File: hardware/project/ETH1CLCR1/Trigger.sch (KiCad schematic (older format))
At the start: 17 parts, among them U401 74AC125, U402 ADuM5402

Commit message: Footprint asigment (not finished).
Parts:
- C402, C404: footprint Capacitor_SMD:C_0603_1608Metric_Pad1.05x0.95mm_HandSolder -> Capacitor_SMD:C_0805_2012Metric_Pad1.15x1.40mm_HandSolder
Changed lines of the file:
@@
 F 0 "C402" H 4465 1196 50  0000 L CNN
 F 1 "1u" H 4465 1105 50  0000 L CNN
-F 2 "Capacitor_SMD:C_0603_1608Metric_Pad1.05x0.95mm_HandSolder" H 4388 1000 50  0001 C CNN
+F 2 "Capacitor_SMD:C_0805_2012Metric_Pad1.15x1.40mm_HandSolder" H 4388 1000 50  0001 C CNN
 F 3 "~" H 4350 1150 50  0001 C CNN
 	1    4350 1150
@@
 F 0 "C404" H 6165 1196 50  0000 L CNN
 F 1 "1u" H 6165 1105 50  0000 L CNN
-F 2 "Capacitor_SMD:C_0603_1608Metric_Pad1.05x0.95mm_HandSolder" H 6088 1000 50  0001 C CNN
+F 2 "Capacitor_SMD:C_0805_2012Metric_Pad1.15x1.40mm_HandSolder" H 6088 1000 50  0001 C CNN
 F 3 "~" H 6050 1150 50  0001 C CNN
 	1    6050 1150

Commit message: Modification in schematic and PCB layout.
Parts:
- added C407, C408: 100n, Capacitor_SMD:C_0603_1608Metric_Pad1.05x0.95mm_HandSolder, symbol Device:C
- added R406: 10k, Resistor_SMD:R_0603_1608Metric_Pad1.05x0.95mm_HandSolder, symbol Device:R
- added U403: TXB0104PW, Package_SO:TSSOP-14_4.4x5mm_P0.65mm, symbol Logic_LevelTranslator:TXB0104PW
- C402, C404: footprint Capacitor_SMD:C_0805_2012Metric_Pad1.15x1.40mm_HandSolder -> Capacitor_SMD:C_0603_1608Metric_Pad1.05x0.95mm_HandSolder
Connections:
- net +3V3: now also C408.1, R406.1, U403.1 (VCCA); no longer C401.1, C402.1, U402.1 (VDD1)
- net GND: now also C407.2, C408.2, U403.7 (GND)
- net TRIG_EN: now also U403.2 (A1); no longer U402.3 (VIA)
- net TRIG_IN: now also U403.4 (A3); no longer U402.5 (VOC)
- net TRIG_OUT: now also U403.3 (A2); no longer U402.4 (VIB)
- new net: U402.3 (VIA), U403.13 (B1)
- new net: U402.4 (VIB), U403.12 (B2)
- new net: U402.5 (VOC), U403.11 (B3)
- new net: R406.2, U403.8 (OE)
- new net +5V: C401.1, C402.1, C407.1, U402.1 (VDD1), U403.14 (VCCB)
- no-connect marks 3 -> 5
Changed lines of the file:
@@
 Wire Wire Line
 	5800 3250 5200 3250
-Text HLabel 4100 3050 0    50   Input ~ 0
+Text HLabel 2650 3050 0    50   Input ~ 0
 TRIG_EN
-Text HLabel 4100 3150 0    50   Input ~ 0
+Text HLabel 2650 3250 0    50   Input ~ 0
 TRIG_OUT
-Text HLabel 4100 3250 0    50   Output ~ 0
+Text HLabel 2650 3450 0    50   Output ~ 0
 TRIG_IN
 Wire Notes Line
@@
 F 0 "C402" H 4465 1196 50  0000 L CNN
 F 1 "1u" H 4465 1105 50  0000 L CNN
-F 2 "Capacitor_SMD:C_0805_2012Metric_Pad1.15x1.40mm_HandSolder" H 4388 1000 50  0001 C CNN
+F 2 "Capacitor_SMD:C_0603_1608Metric_Pad1.05x0.95mm_HandSolder" H 4388 1000 50  0001 C CNN
 F 3 "~" H 4350 1150 50  0001 C CNN
 	1    4350 1150
-	-1   0    0    -1
+	1    0    0    -1
 $EndComp
 $Comp
@@
 F 3 "~" H 3850 1150 50  0001 C CNN
 	1    3850 1150
-	-1   0    0    -1
+	1    0    0    -1
 $EndComp
 Wire Wire Line
@@
 F 0 "C404" H 6165 1196 50  0000 L CNN
 F 1 "1u" H 6165 1105 50  0000 L CNN
-F 2 "Capacitor_SMD:C_0805_2012Metric_Pad1.15x1.40mm_HandSolder" H 6088 1000 50  0001 C CNN
+F 2 "Capacitor_SMD:C_0603_1608Metric_Pad1.05x0.95mm_HandSolder" H 6088 1000 50  0001 C CNN
 F 3 "~" H 6050 1150 50  0001 C CNN
 	1    6050 1150
@@
 	5800 1350 5550 1350
 Wire Wire Line
-	4100 3050 4200 3050
-Wire Wire Line
-	4100 3150 4200 3150
-Wire Wire Line
-	4100 3250 4200 3250
+	2650 3050 2750 3050
+Wire Wire Line
+	2650 3250 2750 3250
+Wire Wire Line
+	2650 3450 2750 3450
 $Comp
 L Device:C C405
@@
 NoConn ~ 4200 3550
 $Comp
-L power:+3.3V #PWR0407
-U 1 1 5EBBBCC5
-P 4500 2650
-F 0 "#PWR0407" H 4500 2500 50  0001 C CNN
-F 1 "+3.3V" H 4515 2823 50  0000 C CNN
-F 2 "" H 4500 2650 50  0001 C CNN
-F 3 "" H 4500 2650 50  0001 C CNN
-	1    4500 2650
-	1    0    0    -1
-$EndComp
-$Comp
-L power:+3.3V #PWR0401
-U 1 1 5EBBC990
-P 4100 900
-F 0 "#PWR0401" H 4100 750 50  0001 C CNN
-F 1 "+3.3V" H 4115 1073 50  0000 C CNN
-F 2 "" H 4100 900 50  0001 C CNN
-F 3 "" H 4100 900 50  0001 C CNN
-	1    4100 900
-	1    0    0    -1
-$EndComp
-$Comp
 L power:GND #PWR0404
 U 1 1 5EBCD574
@@
 	1    0    0    -1
 $EndComp
+$Comp
+L Logic_LevelTranslator:TXB0104PW U?
+U 1 1 5E35DAF4
+P 3150 3350
+AR Path="/5DEEF70B/5E35DAF4" Ref="U?"  Part="1"
+AR Path="/5DEA9498/5E35DAF4" Ref="U403"  Part="1"
+F 0 "U403" H 3650 4100 50  0000 C CNN
+F 1 "TXB0104PW" H 3650 4000 50  0000 C CNN
+F 2 "Package_SO:TSSOP-14_4.4x5mm_P0.65mm" H 3150 2600 50  0001 C CNN
+F 3 "http://www.ti.com/lit/ds/symlink/txb0104.pdf" H 3260 3445 50  0001 C CNN
+	1    3150 3350
+	1    0    0    -1
+$EndComp
+NoConn ~ 2750 3650
+NoConn ~ 3550 3650
+$Comp
+L Device:R R?
+U 1 1 5E35DB02
+P 2550 2650
+AR Path="/5DEEF70B/5E35DB02" Ref="R?"  Part="1"
+AR Path="/5DEA9498/5E35DB02" Ref="R406"  Part="1"
+F 0 "R406" H 2480 2696 50  0000 R CNN
+F 1 "10k" H 2480 2605 50  0000 R CNN
+F 2 "Resistor_SMD:R_0603_1608Metric_Pad1.05x0.95mm_HandSolder" V 2480 2650 50  0001 C CNN
+F 3 "~" H 2550 2650 50  0001 C CNN
+	1    2550 2650
+	1    0    0    -1
+$EndComp
+Wire Wire Line
+	3050 2650 3050 2600
+Wire Wire Line
+	3050 2600 2950 2600
+Wire Wire Line
+	2950 2600 2950 2550
+Wire Wire Line
+	3250 2650 3250 2600
+Wire Wire Line
+	3250 2600 3350 2600
+Wire Wire Line
+	3350 2600 3350 2550
+Wire Wire Line
+	2750 2850 2550 2850
+Wire Wire Line
+	2550 2850 2550 2800
+$Comp
+L power:+3.3V #PWR0407
+U 1 1 5E3798C8
+P 2950 2550
+F 0 "#PWR0407" H 2950 2400 50  0001 C CNN
+F 1 "+3.3V" H 2965 2723 50  0000 C CNN
+F 2 "" H 2950 2550 50  0001 C CNN
+F 3 "" H 2950 2550 50  0001 C CNN
+	1    2950 2550
+	1    0    0    -1
+$EndComp
+$Comp
+L power:+3.3V #PWR0401
+U 1 1 5E37A16A
+P 2550 2500
+F 0 "#PWR0401" H 2550 2350 50  0001 C CNN
+F 1 "+3.3V" H 2565 2673 50  0000 C CNN
+F 2 "" H 2550 2500 50  0001 C CNN
+F 3 "" H 2550 2500 50  0001 C CNN
+	1    2550 2500
+	1    0    0    -1
+$EndComp
+$Comp
+L Device:C C407
+U 1 1 5E381279
+P 2850 1150
+F 0 "C407" H 2965 1196 50  0000 L CNN
+F 1 "100n" H 2965 1105 50  0000 L CNN
+F 2 "Capacitor_SMD:C_0603_1608Metric_Pad1.05x0.95mm_HandSolder" H 2888 1000 50  0001 C CNN
+F 3 "~" H 2850 1150 50  0001 C CNN
+	1    2850 1150
+	1    0    0    -1
+$EndComp
+$Comp
+L Device:C C408
+U 1 1 5E381C99
+P 3350 1150
+F 0 "C408" H 3465 1196 50  0000 L CNN
+F 1 "100n" H 3465 1105 50  0000 L CNN
+F 2 "Capacitor_SMD:C_0603_1608Metric_Pad1.05x0.95mm_HandSolder" H 3388 1000 50  0001 C CNN
+F 3 "~" H 3350 1150 50  0001 C CNN
+	1    3350 1150
+	1    0    0    -1
+$EndComp
+$Comp
+L power:+3.3V #PWR0426
+U 1 1 5E387028
+P 3350 900
+F 0 "#PWR0426" H 3350 750 50  0001 C CNN
+F 1 "+3.3V" H 3365 1073 50  0000 C CNN
+F 2 "" H 3350 900 50  0001 C CNN
+F 3 "" H 3350 900 50  0001 C CNN
+	1    3350 900
+	1    0    0    -1
+$EndComp
+$Comp
+L power:GND #PWR0427
+U 1 1 5E38746C
+P 3350 1400
+F 0 "#PWR0427" H 3350 1150 50  0001 C CNN
+F 1 "GND" H 3355 1227 50  0000 C CNN
+F 2 "" H 3350 1400 50  0001 C CNN
+F 3 "" H 3350 1400 50  0001 C CNN
+	1    3350 1400
+	1    0    0    -1
+$EndComp
+Wire Wire Line
+	3350 900  3350 1000
+Wire Wire Line
+	3350 1300 3350 1400
+$Comp
+L power:+5V #PWR0429
+U 1 1 5E38BA23
+P 4500 2650
+F 0 "#PWR0429" H 4500 2500 50  0001 C CNN
+F 1 "+5V" H 4515 2823 50  0000 C CNN
+F 2 "" H 4500 2650 50  0001 C CNN
+F 3 "" H 4500 2650 50  0001 C CNN
+	1    4500 2650
+	1    0    0    -1
+$EndComp
+$Comp
+L power:+5V #PWR0425
+U 1 1 5E38BD2A
+P 3350 2550
+F 0 "#PWR0425" H 3350 2400 50  0001 C CNN
+F 1 "+5V" H 3365 2723 50  0000 C CNN
+F 2 "" H 3350 2550 50  0001 C CNN
+F 3 "" H 3350 2550 50  0001 C CNN
+	1    3350 2550
+	1    0    0    -1
+$EndComp
+$Comp
+L power:+5V #PWR0423
+U 1 1 5E38C131
+P 2850 900
+F 0 "#PWR0423" H 2850 750 50  0001 C CNN
+F 1 "+5V" H 2865 1073 50  0000 C CNN
+F 2 "" H 2850 900 50  0001 C CNN
+F 3 "" H 2850 900 50  0001 C CNN
+	1    2850 900
+	1    0    0    -1
+$EndComp
+$Comp
+L power:+5V #PWR0428
+U 1 1 5E38CD59
+P 4100 900
+F 0 "#PWR0428" H 4100 750 50  0001 C CNN
+F 1 "+5V" H 4115 1073 50  0000 C CNN
+F 2 "" H 4100 900 50  0001 C CNN
+F 3 "" H 4100 900 50  0001 C CNN
+	1    4100 900
+	1    0    0    -1
+$EndComp
+$Comp
+L power:GND #PWR0424
+U 1 1 5E38D207
+P 2850 1400
+F 0 "#PWR0424" H 2850 1150 50  0001 C CNN
+F 1 "GND" H 2855 1227 50  0000 C CNN
+F 2 "" H 2850 1400 50  0001 C CNN
+F 3 "" H 2850 1400 50  0001 C CNN
+	1    2850 1400
+	1    0    0    -1
+$EndComp
+Wire Wire Line
+	2850 1400 2850 1300
+Wire Wire Line
+	2850 1000 2850 900
+$Comp
+L power:GND #PWR0106
+U 1 1 5E39EC61
+P 3150 4050
+F 0 "#PWR0106" H 3150 3800 50  0001 C CNN
+F 1 "GND" H 3155 3877 50  0000 C CNN
+F 2 "" H 3150 4050 50  0001 C CNN
+F 3 "" H 3150 4050 50  0001 C CNN
+	1    3150 4050
+	1    0    0    -1
+$EndComp
+Wire Wire Line
+	3550 3050 4200 3050
+Wire Wire Line
+	4200 3150 3700 3150
+Wire Wire Line
+	3700 3150 3700 3250
+Wire Wire Line
+	3700 3250 3550 3250
+Wire Wire Line
+	3550 3450 3800 3450
+Wire Wire Line
+	3800 3450 3800 3250
+Wire Wire Line
+	3800 3250 4200 3250
 $EndSCHEMATC

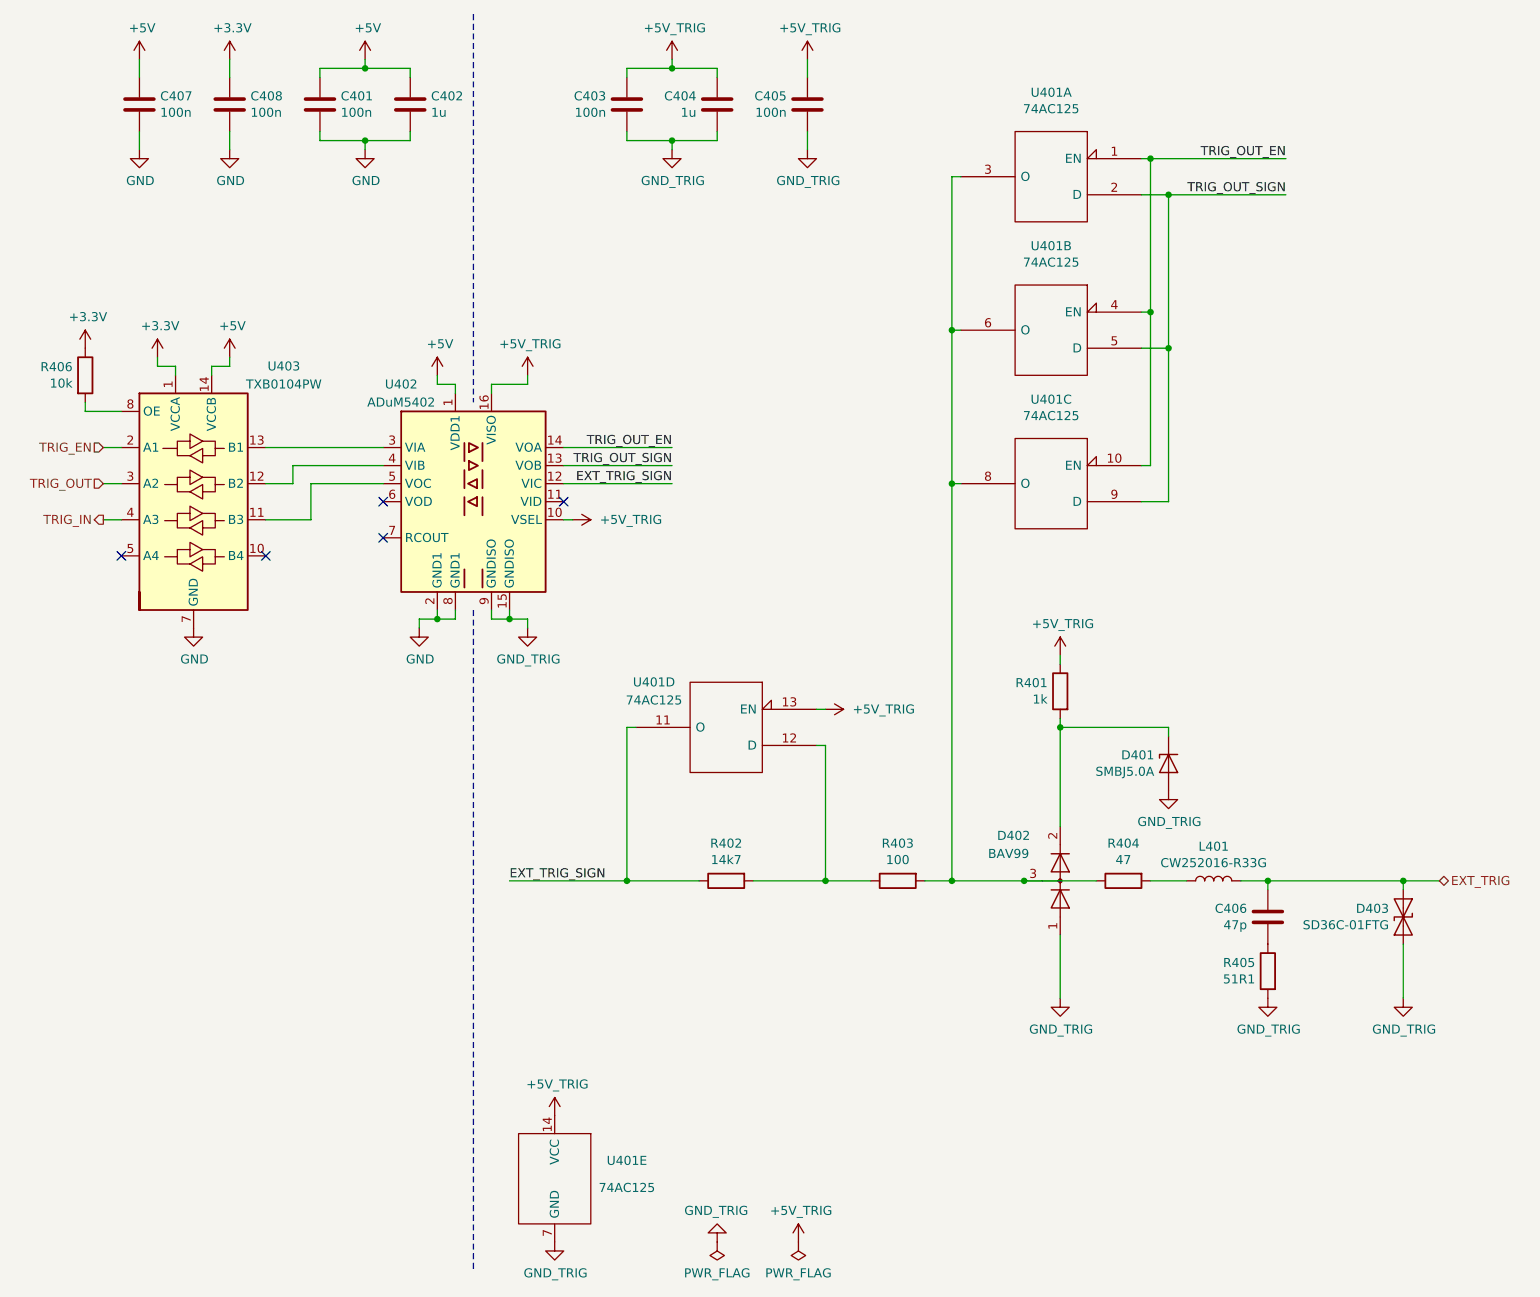
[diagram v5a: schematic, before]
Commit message: Redesinged ADC schematic.
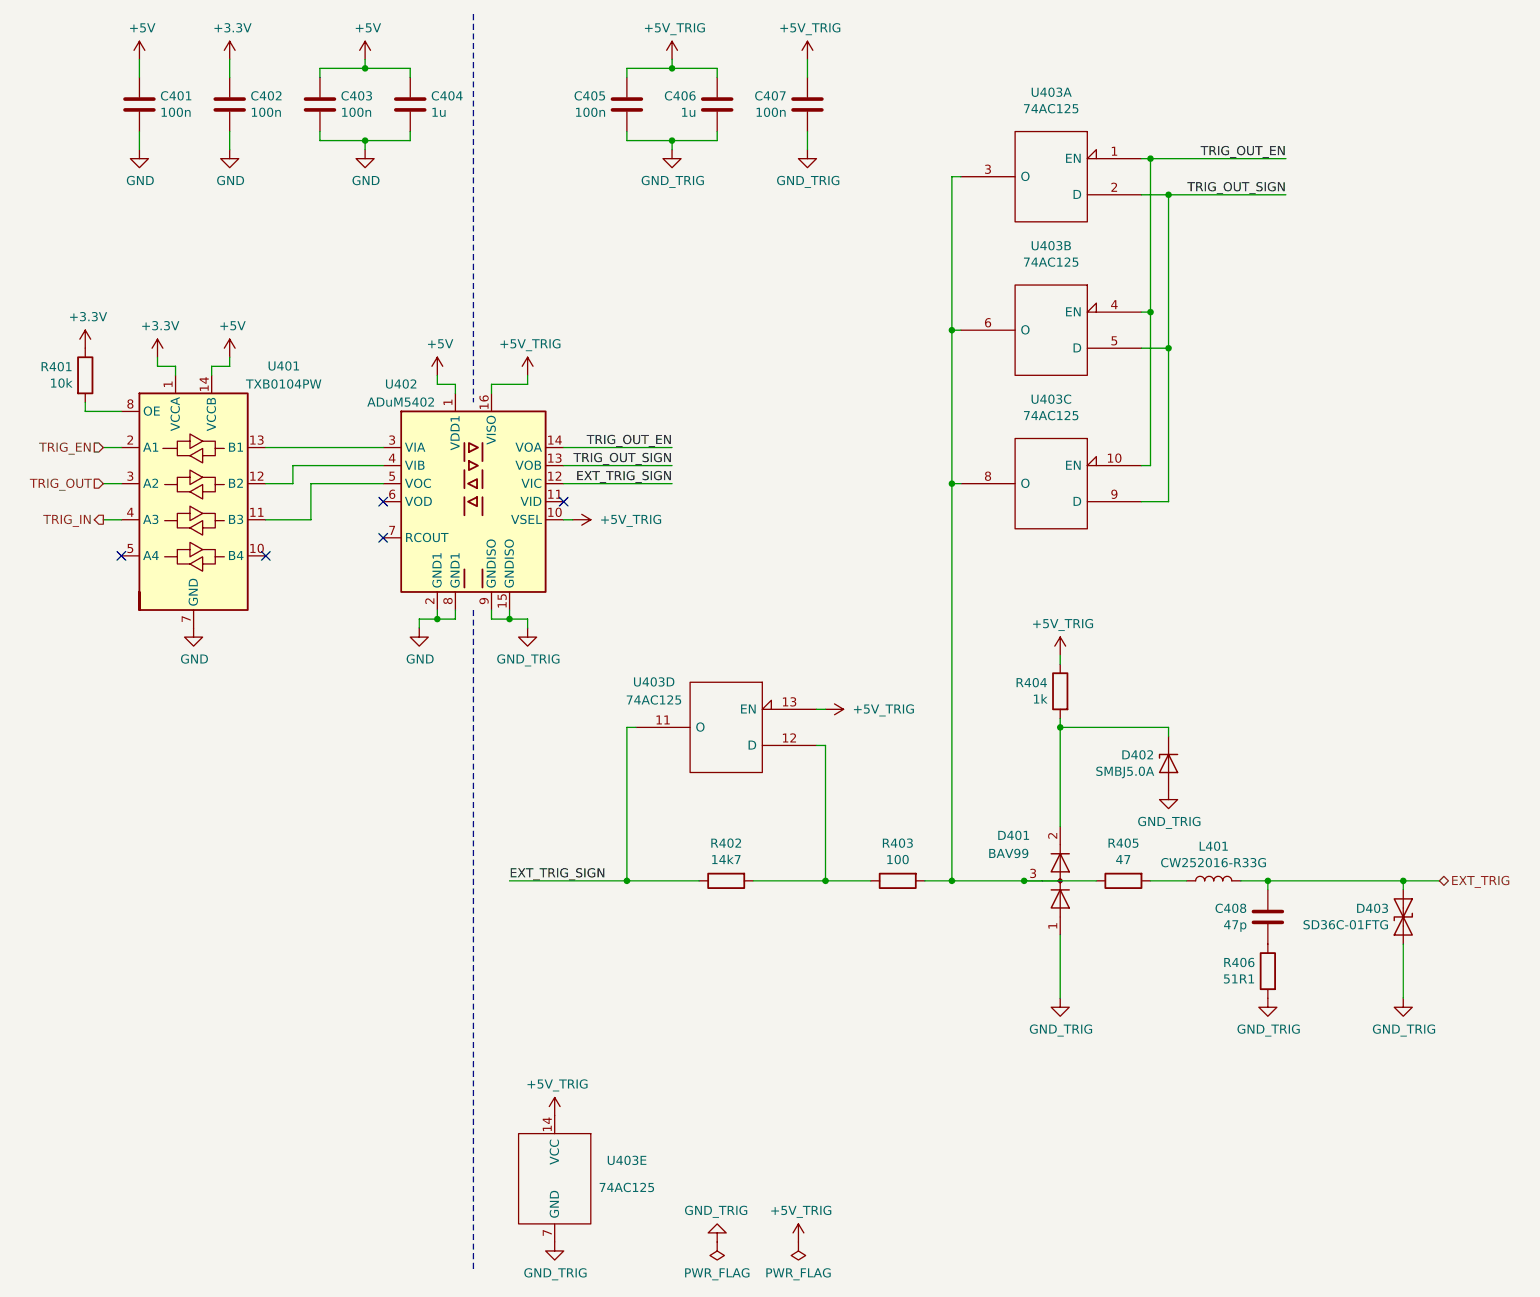
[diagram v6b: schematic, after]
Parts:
- renumbered C407 to C401, C408 to C402, C401 to C403, C402 to C404, C403 to C405, C404 to C406, C405 to C407, C406 to C408, D402 to D401, D401 to D402, R406 to R401, R401 to R404, R404 to R405, R405 to R406, U403 to U401, U401 to U403

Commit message: PCB done.
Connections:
- net +5V_TRIG: no longer U403.13 (EN)
- net EXT_TRIG_SIGN: now also U403.3 (O); no longer U403.11 (O)
- net GND_TRIG: now also U403.1 (EN)
- net TRIG_OUT_EN: now also U403.13 (EN); no longer U403.1 (EN)
- net TRIG_OUT_SIGN: now also U403.12 (D); no longer U403.2 (D)
- net at D401.3 (K), R403.2, R405.1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: now also U403.11 (O); no longer U403.3 (O)
- net at R402.2, R403.1: now also U403.2 (D); no longer U403.12 (D)
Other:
- moved on the sheet: U403A, U403B, U403C, U403D
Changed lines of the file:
@@
 L ETH1CLCR1:74AC125 U403
 U 3 1 5D9C7DE2
-P 7900 3250
-F 0 "U403" H 7900 3716 50  0000 C CNN
-F 1 "74AC125" H 7900 3625 50  0000 C CNN
-F 2 "Package_SO:TSSOP-14_4.4x5mm_P0.65mm" H 7900 3250 50  0001 C CNN
-F 3 "" H 7900 3250 50  0001 C CNN
-	3    7900 3250
+P 7900 2400
+F 0 "U403" H 7900 2866 50  0000 C CNN
+F 1 "74AC125" H 7900 2775 50  0000 C CNN
+F 2 "Package_SO:TSSOP-14_4.4x5mm_P0.65mm" H 7900 2400 50  0001 C CNN
+F 3 "" H 7900 2400 50  0001 C CNN
+	3    7900 2400
 	-1   0    0    -1
 $EndComp
@@
 L ETH1CLCR1:74AC125 U403
 U 4 1 5D218310
-P 6100 4600
-F 0 "U403" H 6500 4850 50  0000 C CNN
-F 1 "74AC125" H 6500 4750 50  0000 C CNN
-F 2 "Package_SO:TSSOP-14_4.4x5mm_P0.65mm" H 6100 4600 50  0001 C CNN
-F 3 "" H 6100 4600 50  0001 C CNN
-	4    6100 4600
+P 7900 3250
+F 0 "U403" H 7900 3700 50  0000 C CNN
+F 1 "74AC125" H 7900 3600 50  0000 C CNN
+F 2 "Package_SO:TSSOP-14_4.4x5mm_P0.65mm" H 7900 3250 50  0001 C CNN
+F 3 "" H 7900 3250 50  0001 C CNN
+	4    7900 3250
 	-1   0    0    -1
 $EndComp
@@
 L ETH1CLCR1:74AC125 U403
 U 2 1 5D2189A9
-P 7900 2400
-F 0 "U403" H 7900 2866 50  0000 C CNN
-F 1 "74AC125" H 7900 2775 50  0000 C CNN
-F 2 "Package_SO:TSSOP-14_4.4x5mm_P0.65mm" H 7900 2400 50  0001 C CNN
-F 3 "" H 7900 2400 50  0001 C CNN
-	2    7900 2400
-	-1   0    0    -1
-$EndComp
-$Comp
-L ETH1CLCR1:74AC125 U403
-U 1 1 5D21AD13
 P 7900 1550
 F 0 "U403" H 7900 2016 50  0000 C CNN
@@
 F 2 "Package_SO:TSSOP-14_4.4x5mm_P0.65mm" H 7900 1550 50  0001 C CNN
 F 3 "" H 7900 1550 50  0001 C CNN
-	1    7900 1550
+	2    7900 1550
+	-1   0    0    -1
+$EndComp
+$Comp
+L ETH1CLCR1:74AC125 U403
+U 1 1 5D21AD13
+P 6100 4600
+F 0 "U403" H 6100 5066 50  0000 C CNN
+F 1 "74AC125" H 6100 4975 50  0000 C CNN
+F 2 "Package_SO:TSSOP-14_4.4x5mm_P0.65mm" H 6100 4600 50  0001 C CNN
+F 3 "" H 6100 4600 50  0001 C CNN
+	1    6100 4600
 	-1   0    0    -1
 $EndComp
@@
 Wire Wire Line
 	7200 5450 7350 5450
-Wire Wire Line
-	6650 4500 6600 4500
 Wire Wire Line
 	6600 4700 6650 4700
@@
 $EndComp
 $Comp
-L ETH1CLCR1:+5V_TRIG #PWR0424
-U 1 1 5EBE6C8E
-P 6650 4500
-F 0 "#PWR0424" H 6650 4350 50  0001 C CNN
-F 1 "+5V_TRIG" V 6650 4650 50  0000 L CNN
-F 2 "" H 6650 4500 50  0001 C CNN
-F 3 "" H 6650 4500 50  0001 C CNN
-	1    6650 4500
-	0    1    1    0
-$EndComp
-$Comp
 L ETH1CLCR1:+5V_TRIG #PWR0425
 U 1 1 5EBE9033
@@
 Wire Wire Line
 	3800 3250 4200 3250
+$Comp
+L ETH1CLCR1:GND_TRIG #PWR0108
+U 1 1 5E9AD50E
+P 6600 4500
+F 0 "#PWR0108" H 6600 4250 50  0001 C CNN
+F 1 "GND_TRIG" V 6600 4200 50  0000 C CNN
+F 2 "" H 6600 4500 50  0001 C CNN
+F 3 "" H 6600 4500 50  0001 C CNN
+	1    6600 4500
+	0    -1   -1   0
+$EndComp
 $EndSCHEMATC
